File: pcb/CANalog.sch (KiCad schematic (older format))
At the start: 93 parts, among them J1 PWR, J2 USB_B_Micro, J3 SPI3, J4 I2C2, J5 STM_PROG, J6 ESP_PROG, J7 AOUT, J8 CAN, Q1 DMP3099L-7, Q2 MMBT2222A, Q3 DMP3099L-7, SW1 ESP_PROG, SW2 RESET, U1 BL9342, U2 RS321BXF, U3 STM32F302C8T6, U4 MIC5504-3.3YM5, U5 ESP-12F, U6 OPA330xxDBV, U7 74AHC1G66, U8 SN65HVD230, Y1 16MHz

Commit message: add CAN terminal footprint
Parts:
- J8: footprint (none) -> pl_TerminalBlock:WJ127-5.0-3P
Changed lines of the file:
@@
 F 0 "J8" H 16200 2200 50  0000 C CNN
 F 1 "CAN" H 16200 1800 50  0000 C CNN
-F 2 "" H 16200 2000 50  0001 C CNN
+F 2 "pl_TerminalBlock:WJ127-5.0-3P" H 16200 2000 50  0001 C CNN
 F 3 "https://datasheet.lcsc.com/szlcsc/1912251633_Ningbo-Kangnex-Elec-WJ127-5-0-3P_C8393.pdf" H 16200 2000 50  0001 C CNN
 F 4 "WJ127-5.0-3P" H 16200 2000 50  0001 C CNN "MPN"

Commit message: add remaining footprints
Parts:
- JP?: footprint (none) -> Jumper:SolderJumper-3_P1.3mm_Bridged2Bar12_Pad1.0x1.5mm
- Y1: footprint (none) -> Crystal:Resonator_SMD_muRata_CSTxExxV-3Pin_3.0x1.1mm
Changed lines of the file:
@@
 F 0 "Y1" H 6650 6425 50  0000 C CNN
 F 1 "16MHz" H 6650 6350 50  0000 C CNN
-F 2 "" H 6625 6200 50  0001 C CNN
+F 2 "Crystal:Resonator_SMD_muRata_CSTxExxV-3Pin_3.0x1.1mm" H 6625 6200 50  0001 C CNN
 F 3 "https://www.mouser.com/datasheet/2/281/murata_04192018_CSTN_CeramResonCERAL-1323383.pdf" H 6625 6200 50  0001 C CNN
 F 4 "DNP" V 6650 6200 50  0000 C CNN "Population"
@@
 F 0 "JP?" H 12150 900 50  0000 C CNN
 F 1 "PSELECT" H 12250 1110 50  0000 C CNN
-F 2 "" H 12250 1000 50  0001 C CNN
+F 2 "Jumper:SolderJumper-3_P1.3mm_Bridged2Bar12_Pad1.0x1.5mm" H 12250 1000 50  0001 C CNN
 F 3 "~" H 12250 1000 50  0001 C CNN
 	1    12250 1000

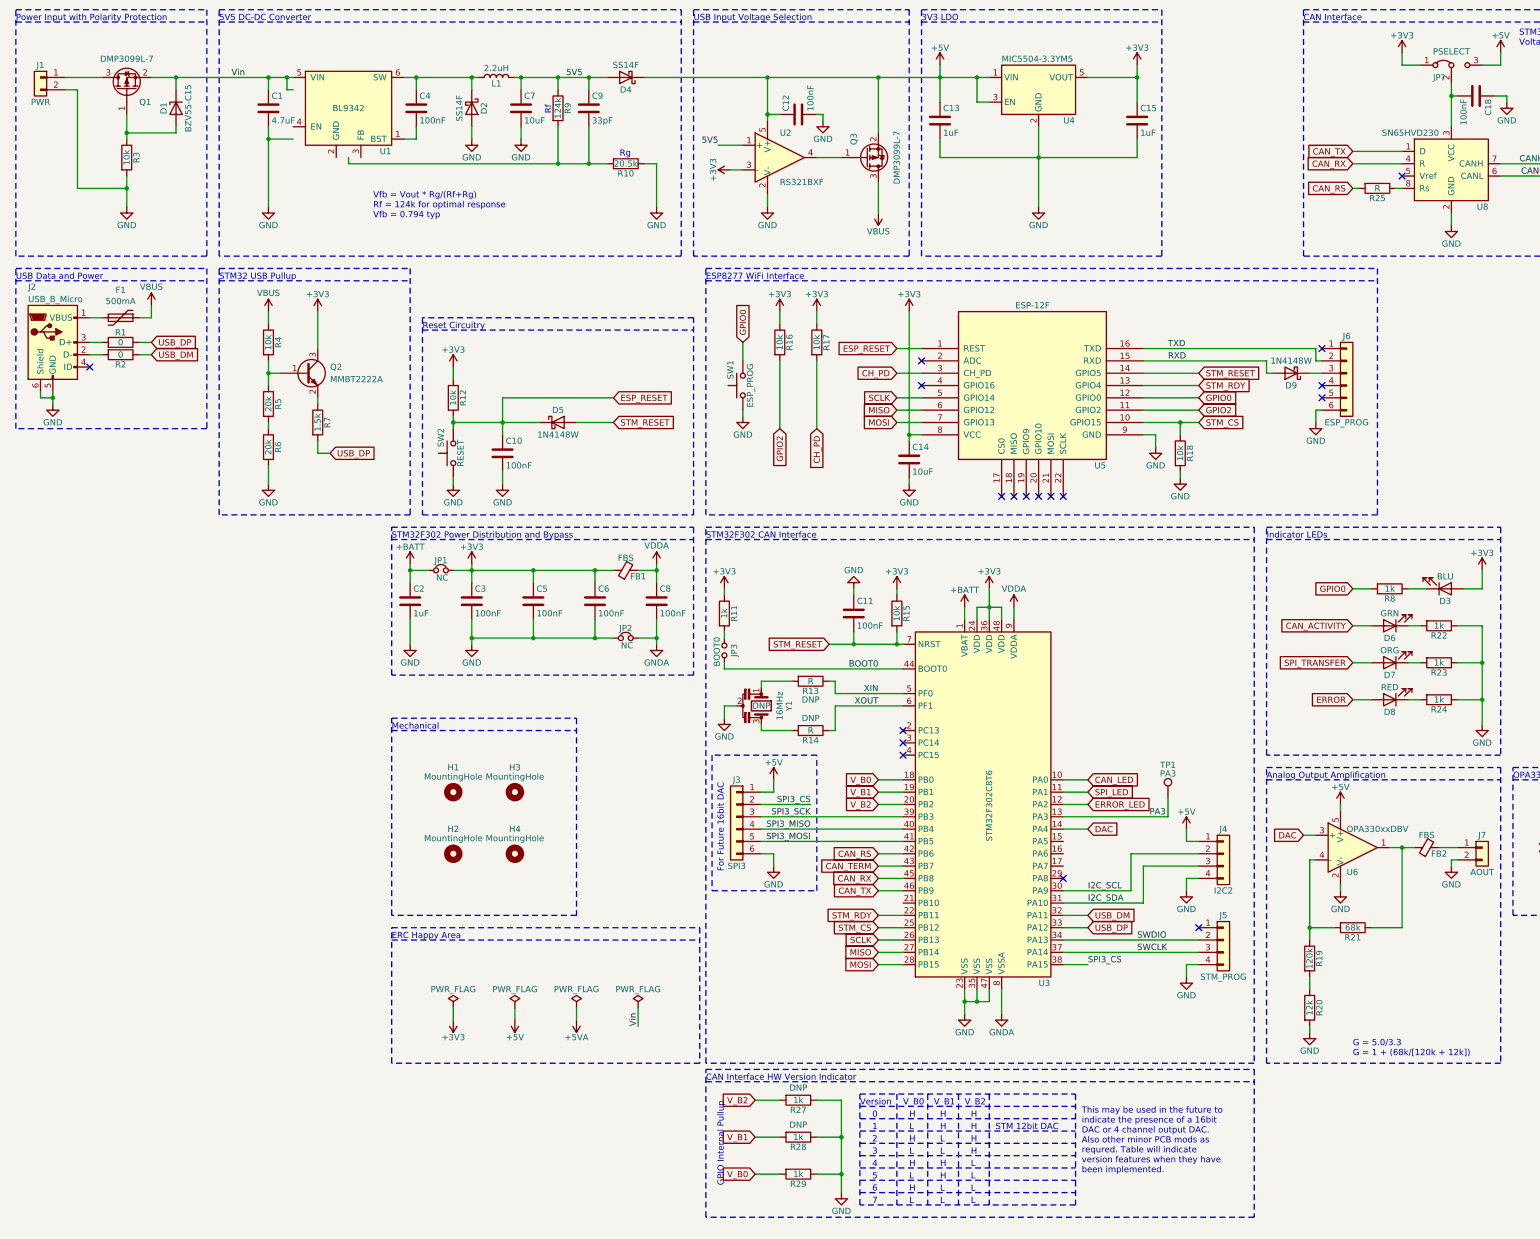
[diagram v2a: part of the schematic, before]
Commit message: erc cleanup
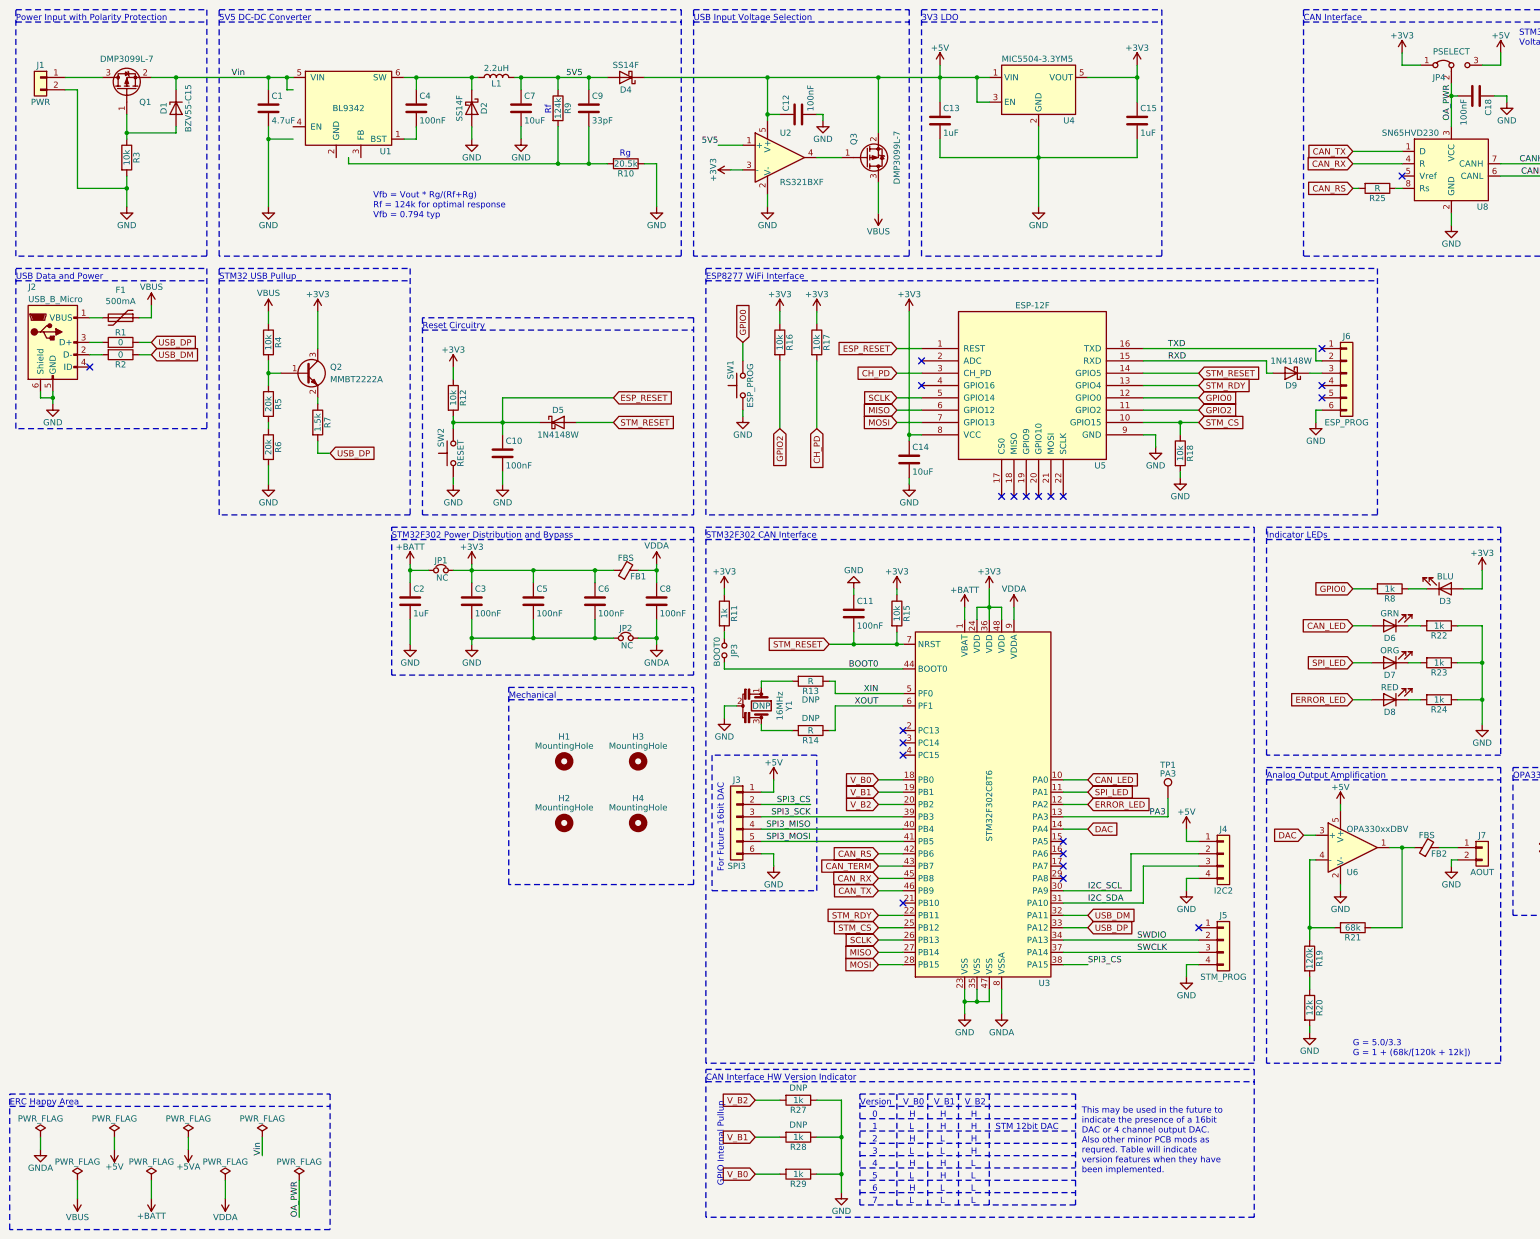
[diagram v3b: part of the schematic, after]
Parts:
- gave numbers to parts that had none: 1
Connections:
- net CAN_ACTIVITY is gone; now on net CAN_LED: D6.2 (A)
- net ERROR is gone; now on net ERROR_LED: D8.2 (A)
- net SPI_TRANSFER is gone; now on net SPI_LED: D7.2 (A)
- net OA_PWR: now reaches C18.2, JP4.2 (C), U8.3 (VCC)
- no-connect marks 18 -> 22
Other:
- moved on the sheet: H1, H2, H3, H4

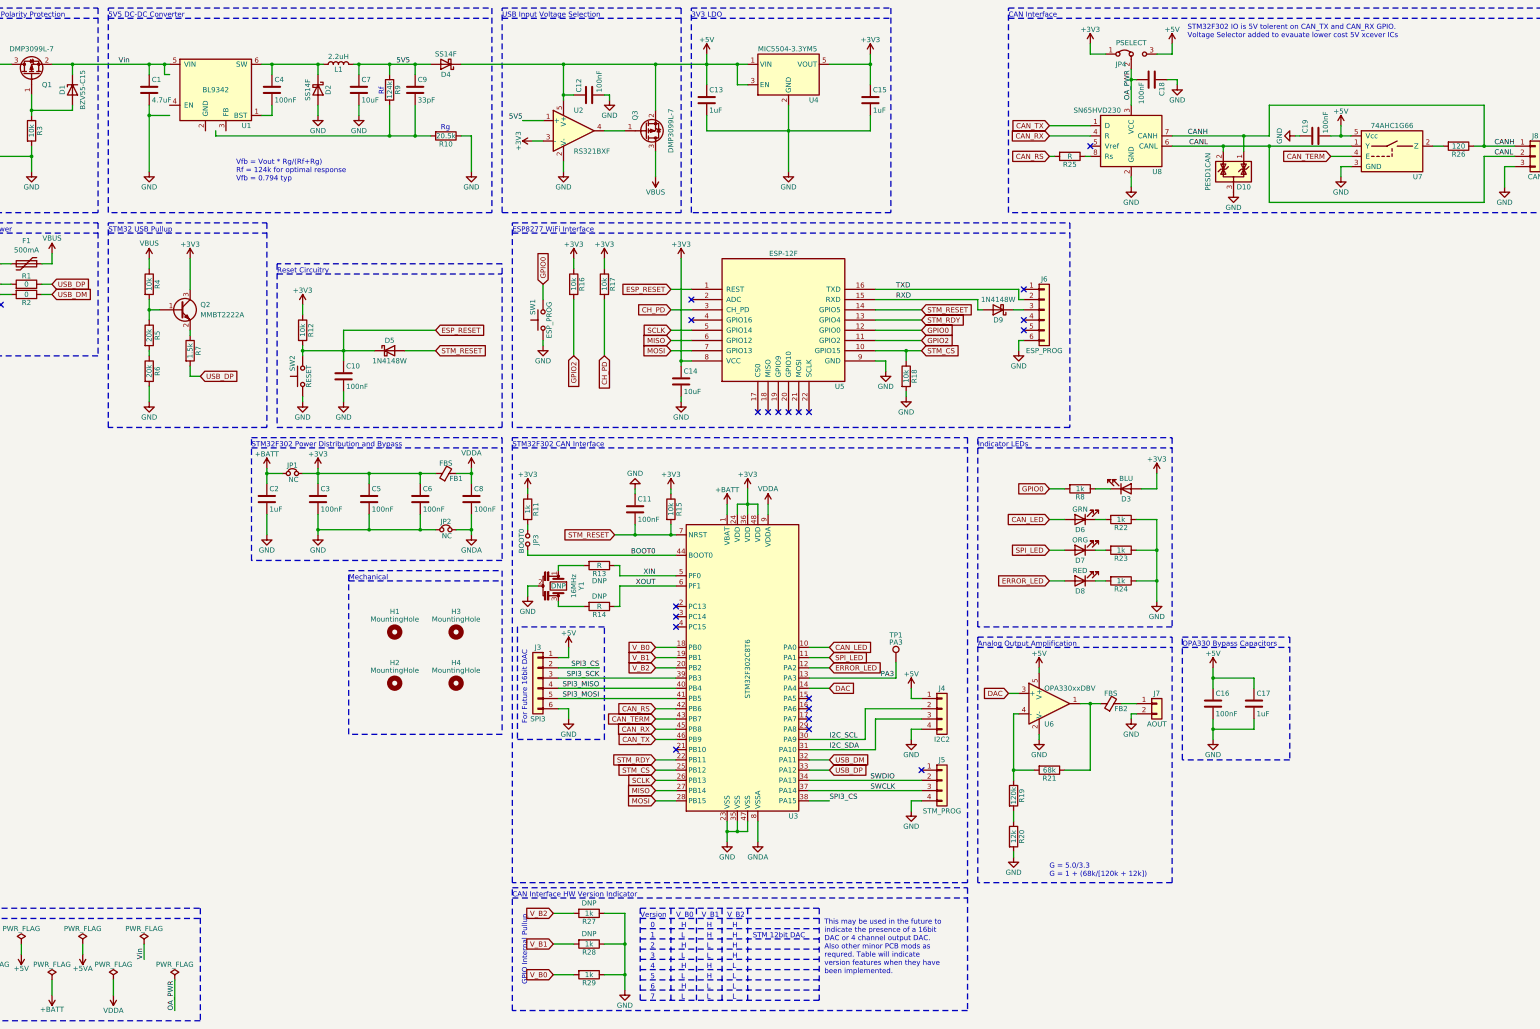
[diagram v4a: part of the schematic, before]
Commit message: add overvoltage protection to BL9342 enable pin
this pin cannot exceed 5V!!!! Learned this the hard way but best to learn it now with the nucleo prototype. RIP dev board.
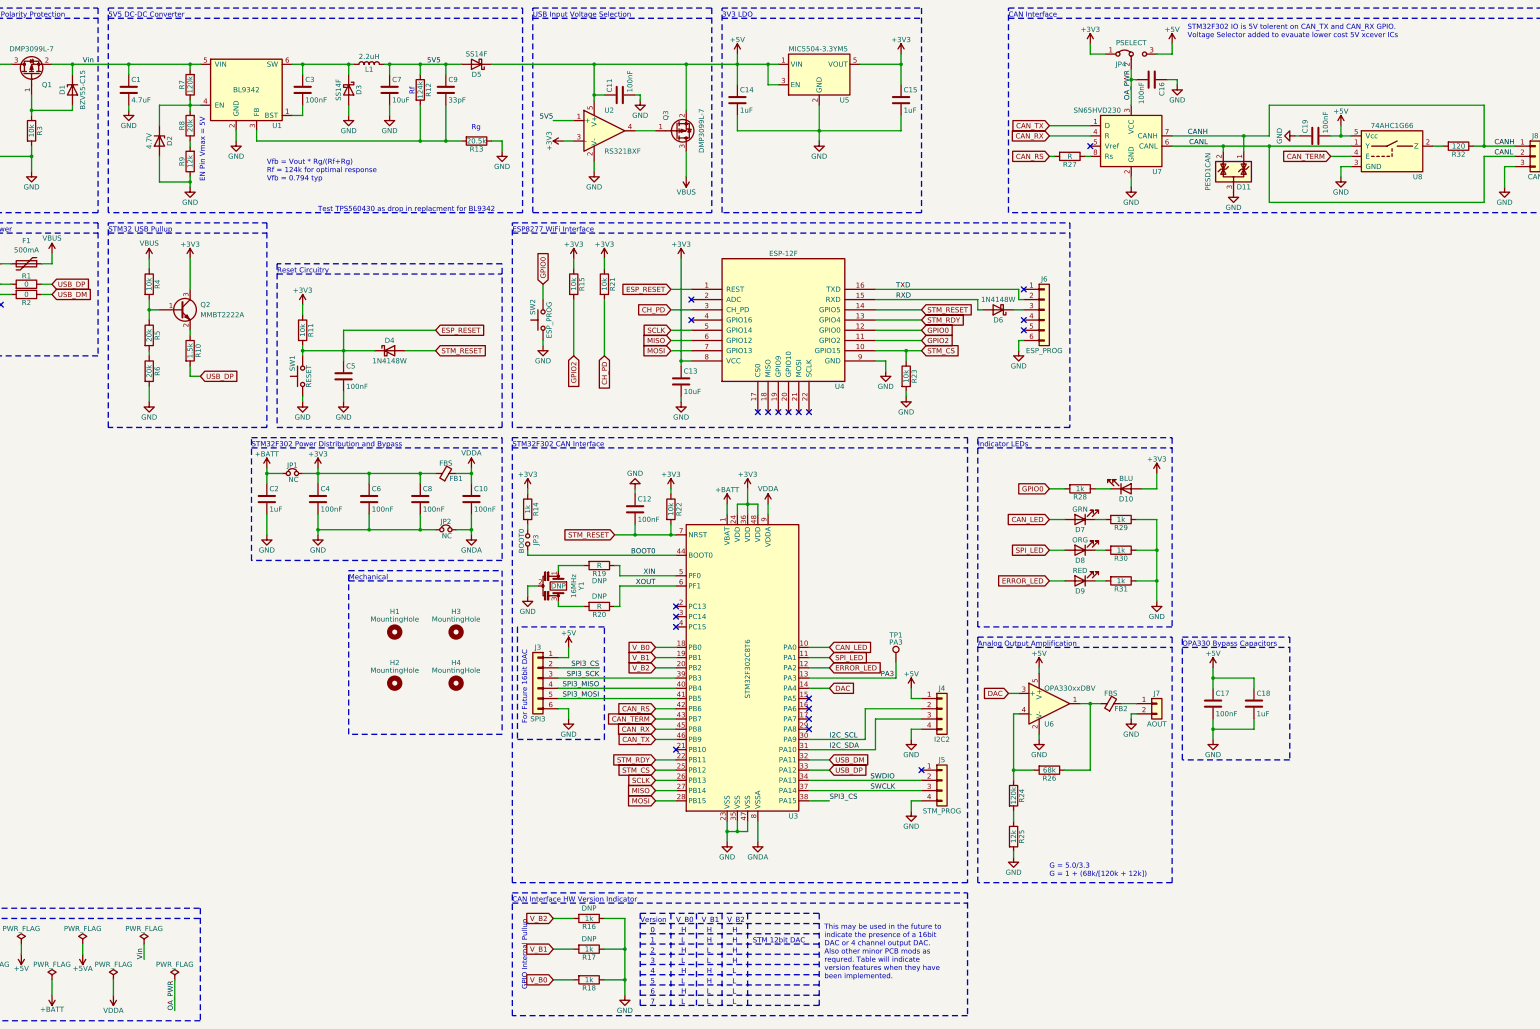
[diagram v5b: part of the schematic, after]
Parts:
- added D2: 4.7V, Diode_SMD:D_SOD-123, symbol Device:D_Zener
- added R7: 120k, Resistor_SMD:R_0603_1608Metric, symbol Device:R
- added R8: 20k, Resistor_SMD:R_0603_1608Metric, symbol Device:R
- added R9: 12k, Resistor_SMD:R_0603_1608Metric, symbol Device:R
- renumbered C8 to C10, C12 to C11, C11 to C12, C14 to C13, C13 to C14, C18 to C16, C16 to C17, C17 to C18, C4 to C3, C3 to C4, C10 to C5, C5 to C6, C6 to C8, D3 to D10, D10 to D11, D2 to D3, D5 to D4, D4 to D5, D9 to D6, D6 to D7, D7 to D8, D8 to D9, R7 to R10, R12 to R11, R9 to R12, R10 to R13, R11 to R14, R16 to R15, R27 to R16, R28 to R17, R29 to R18, R13 to R19, R14 to R20, R17 to R21, R15 to R22, R18 to R23, R19 to R24, R20 to R25, R21 to R26, R25 to R27, R8 to R28, R22 to R29, R23 to R30, R24 to R31, R26 to R32, SW2 to SW1, SW1 to SW2, U5 to U4, U4 to U5, U8 to U7, U7 to U8
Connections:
- net GND: now also U1.2 (GND), D2.2 (A), R9.1
- net Vin: now also R7.2
- net at U1.3 (FB): now also C9.2, R12.2, R13.2
- net at U1.4 (EN): now also D2.1 (K), R7.1, R8.2
- new net: R8.1, R9.2
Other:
- note added: "EN Pin Vmax = 5V"
- note added: "Test TPS560430 as drop in replacment for BL9342"
- moved on the sheet: C1, C11, C14, C15, C3, C7, C9, D3, D5, L1, Q3, R12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
